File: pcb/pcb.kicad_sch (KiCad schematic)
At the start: 3 parts, among them U2 ESP32-C6-MINI-1

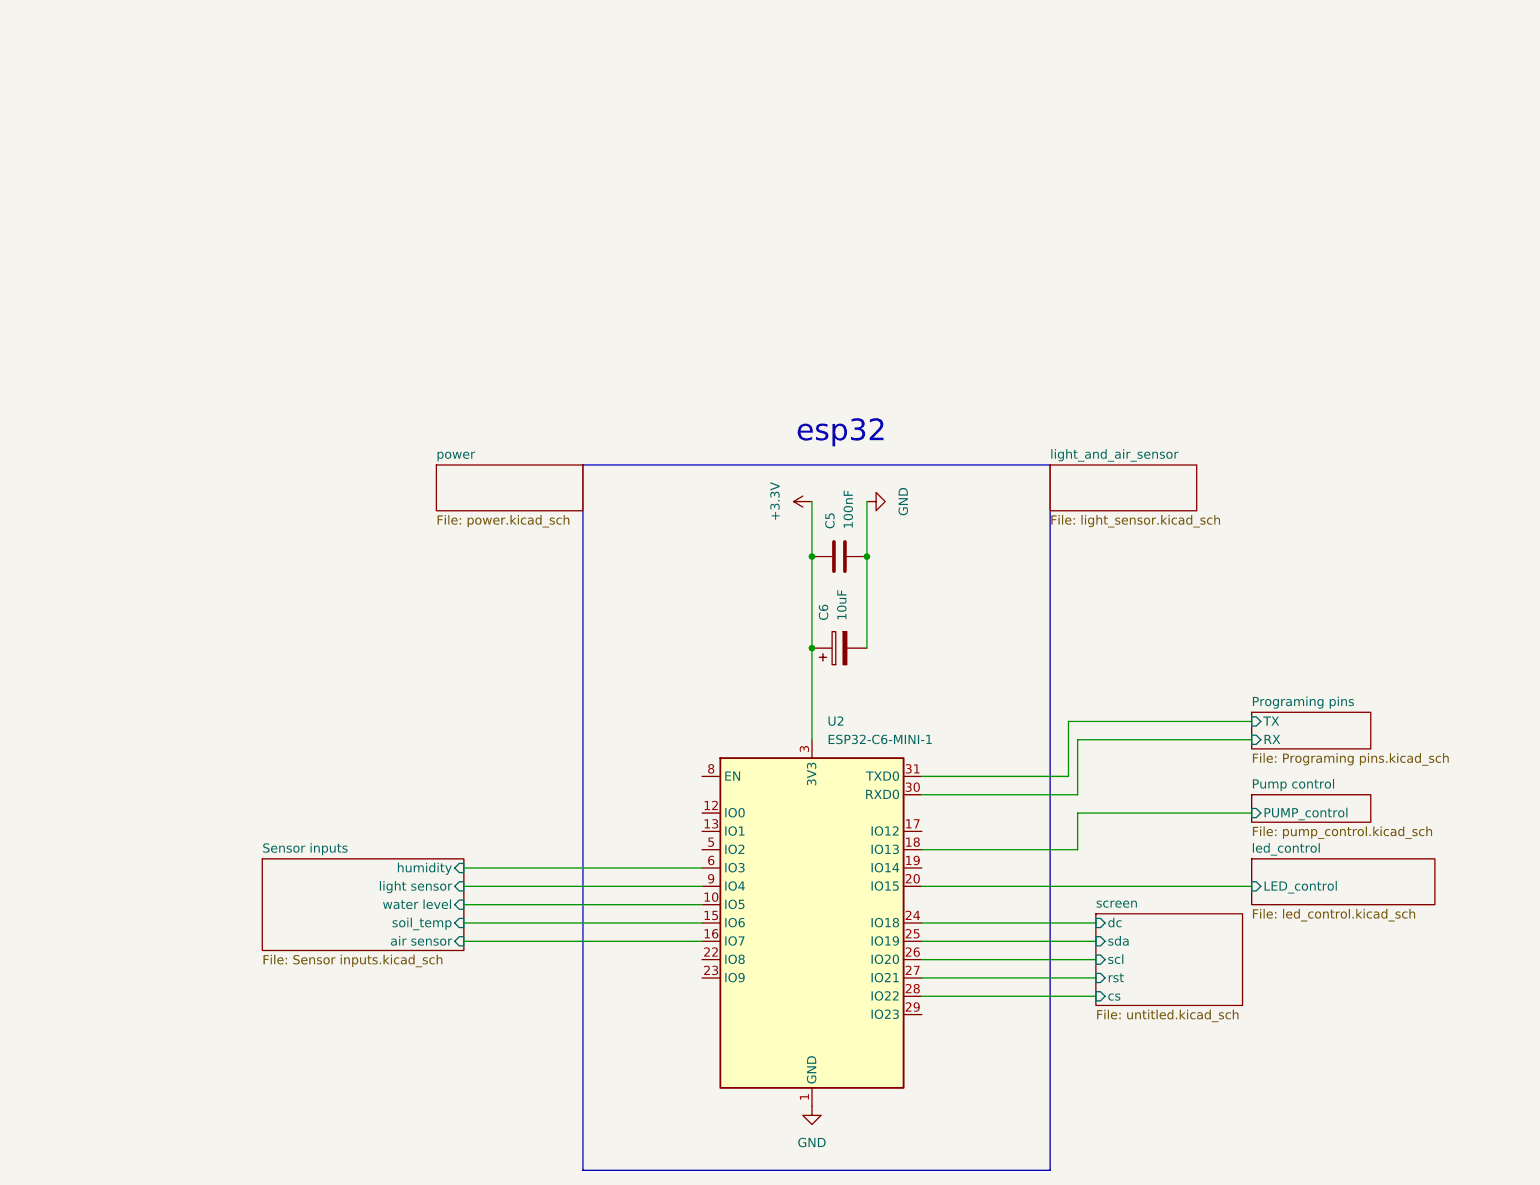
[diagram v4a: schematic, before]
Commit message: trieing to make a 3d model from the shematic and fixing some issues about the esp32 gipos
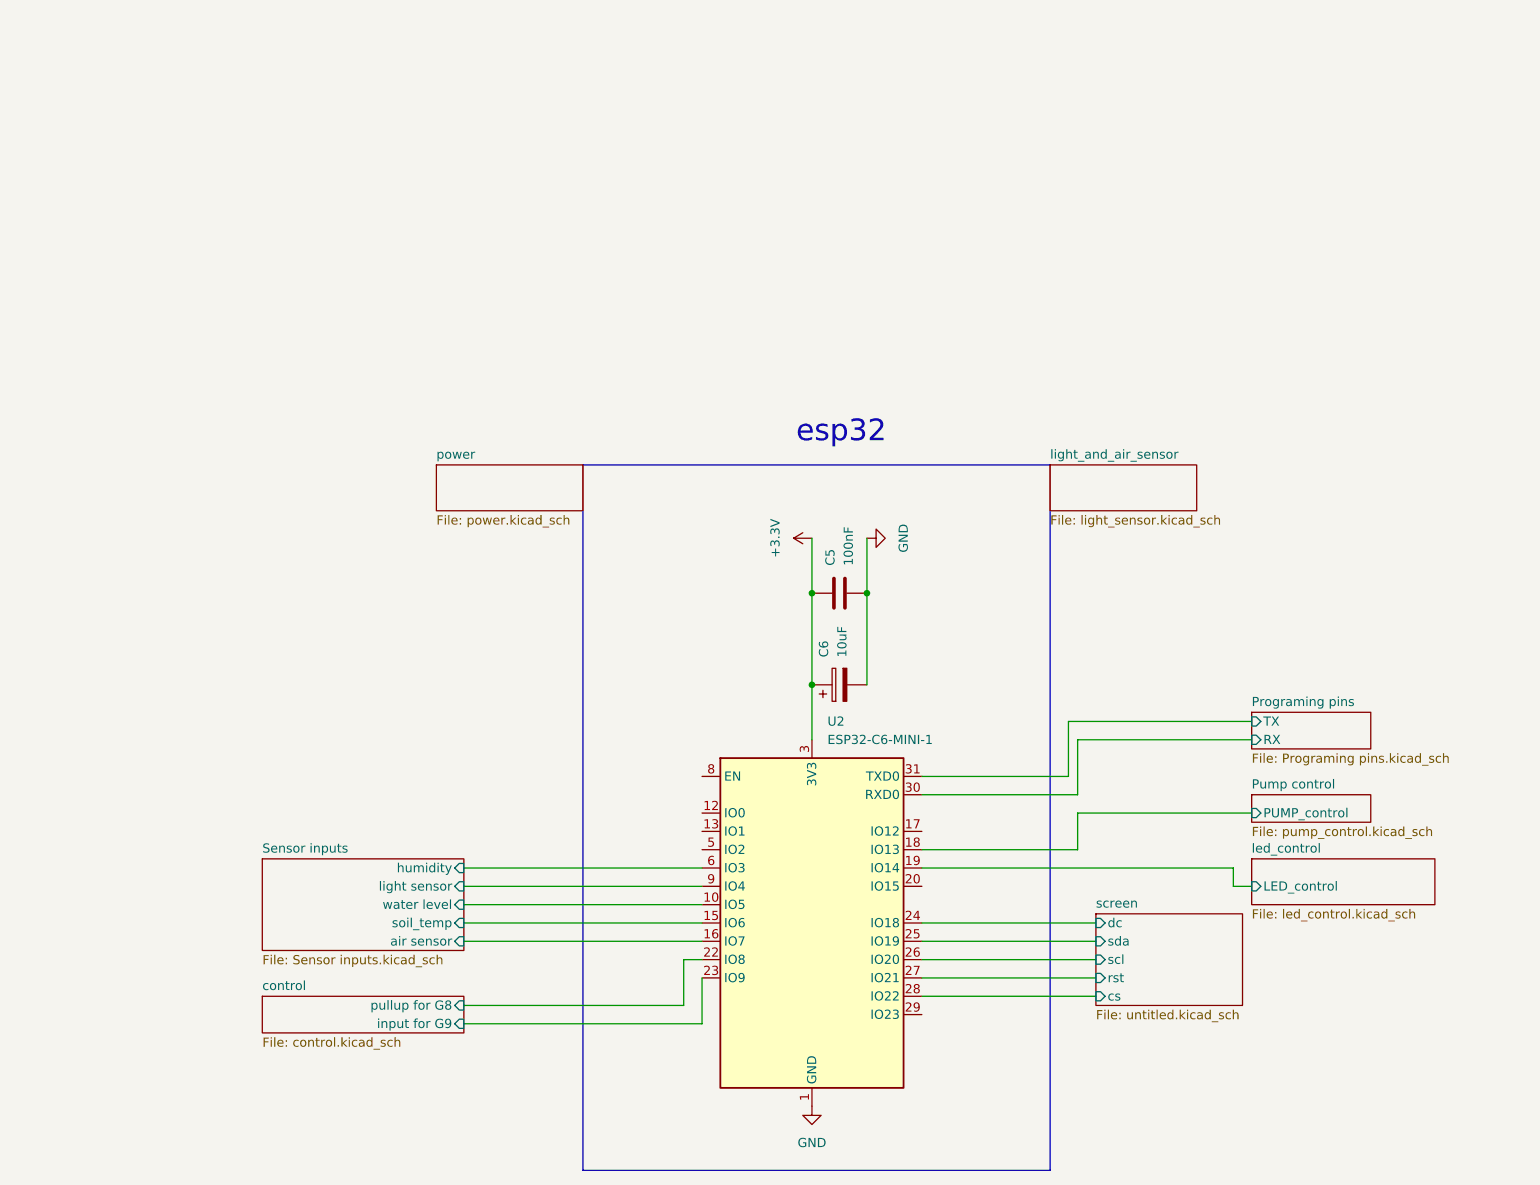
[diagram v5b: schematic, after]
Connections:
- net led_control/LED_control: now also U2.19 (IO14); no longer U2.20 (IO15)
- net control/pullup for G8: now reaches U2.22 (IO8)
- net control/input for G9: now reaches U2.23 (IO9)
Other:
- added sheet control (control.kicad_sch)
- moved on the sheet: C5, C6
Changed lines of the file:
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@@
 	)
 	(junction
-		(at 137.16 91.44)
+		(at 137.16 96.52)
 		(diameter 0)
 		(color 0 0 0 0)
 	)
 	(junction
-		(at 129.54 91.44)
+		(at 129.54 96.52)
 		(diameter 0)
 		(color 0 0 0 0)
 	)
 	(junction
-		(at 129.54 104.14)
+		(at 129.54 109.22)
 		(diameter 0)
 		(color 0 0 0 0)
@@
 	(wire
 		(pts
-			(xy 129.54 104.14) (xy 129.54 116.84)
+			(xy 129.54 109.22) (xy 129.54 116.84)
+		)
+		(stroke
+			(width 0)
+			(type default)
+		)
+	)
+	(wire
+		(pts
+			(xy 111.76 147.32) (xy 111.76 153.67)
 		)
 		(stroke
@@
 	(wire
 		(pts
+			(xy 187.96 134.62) (xy 187.96 137.16)
+		)
+		(stroke
+			(width 0)
+			(type default)
+		)
+	)
+	(wire
+		(pts
 			(xy 166.37 116.84) (xy 166.37 124.46)
 		)
@@
 	(wire
 		(pts
+			(xy 81.28 156.21) (xy 114.3 156.21)
+		)
+		(stroke
+			(width 0)
+			(type default)
+		)
+	)
+	(wire
+		(pts
+			(xy 114.3 147.32) (xy 111.76 147.32)
+		)
+		(stroke
+			(width 0)
+			(type default)
+		)
+	)
+	(wire
+		(pts
+			(xy 187.96 137.16) (xy 190.5 137.16)
+		)
+		(stroke
+			(width 0)
+			(type default)
+		)
+	)
+	(wire
+		(pts
 			(xy 144.78 152.4) (xy 168.91 152.4)
 		)
@@
 	(wire
 		(pts
-			(xy 129.54 91.44) (xy 129.54 104.14)
+			(xy 129.54 96.52) (xy 129.54 109.22)
 		)
 		(stroke
@@
 	(wire
 		(pts
-			(xy 137.16 91.44) (xy 137.16 104.14)
+			(xy 114.3 156.21) (xy 114.3 149.86)
+		)
+		(stroke
+			(width 0)
+			(type default)
+		)
+	)
+	(wire
+		(pts
+			(xy 137.16 96.52) (xy 137.16 109.22)
 		)
 		(stroke
@@
 	(wire
 		(pts
-			(xy 144.78 137.16) (xy 190.5 137.16)
-		)
-		(stroke
-			(width 0)
-			(type default)
-		)
-	)
-	(wire
-		(pts
 			(xy 165.1 114.3) (xy 165.1 121.92)
 		)
@@
 	(wire
 		(pts
-			(xy 129.54 83.82) (xy 129.54 91.44)
-		)
-		(stroke
-			(width 0)
-			(type default)
-		)
-	)
-	(wire
-		(pts
-			(xy 137.16 83.82) (xy 137.16 91.44)
+			(xy 129.54 88.9) (xy 129.54 96.52)
+		)
+		(stroke
+			(width 0)
+			(type default)
+		)
+	)
+	(wire
+		(pts
+			(xy 81.28 153.67) (xy 111.76 153.67)
+		)
+		(stroke
+			(width 0)
+			(type default)
+		)
+	)
+	(wire
+		(pts
+			(xy 144.78 134.62) (xy 187.96 134.62)
+		)
+		(stroke
+			(width 0)
+			(type default)
+		)
+	)
+	(wire
+		(pts
+			(xy 137.16 88.9) (xy 137.16 96.52)
 		)
 		(stroke
@@
 	(symbol
 		(lib_id "power:GND")
-		(at 137.16 83.82 90)
+		(at 137.16 88.9 90)
 		(unit 1)
 		(exclude_from_sim no)
@@
 		(fields_autoplaced yes)
 		(property "Reference" "#PWR04"
-			(at 143.51 83.82 0)
+			(at 143.51 88.9 0)
 			(effects
 				(font
@@
 		)
 		(property "Value" "GND"
-			(at 142.24 83.82 0)
+			(at 142.24 88.9 0)
 			(effects
 				(font
@@
 		)
 		(property "Footprint" ""
-			(at 137.16 83.82 0)
+			(at 137.16 88.9 0)
 			(effects
 				(font
@@
 		)
 		(property "Datasheet" ""
-			(at 137.16 83.82 0)
+			(at 137.16 88.9 0)
 			(effects
 				(font
@@
 		)
 		(property "Description" "Power symbol creates a global label with name \"GND\" , ground"
-			(at 137.16 83.82 0)
+			(at 137.16 88.9 0)
 			(effects
 				(font
@@
 	(symbol
 		(lib_id "Device:C_Polarized")
-		(at 133.35 104.14 90)
+		(at 133.35 109.22 90)
 		(unit 1)
 		(exclude_from_sim no)
@@
 		(fields_autoplaced yes)
 		(property "Reference" "C6"
-			(at 131.1909 100.33 0)
+			(at 131.1909 105.41 0)
 			(effects
 				(font
@@
 		)
 		(property "Value" "10uF"
-			(at 133.7309 100.33 0)
+			(at 133.7309 105.41 0)
 			(effects
 				(font
@@
 		)
 		(property "Footprint" "Capacitor_THT:CP_Radial_D5.0mm_P2.50mm"
-			(at 137.16 103.1748 0)
+			(at 137.16 108.2548 0)
 			(effects
 				(font
@@
 		)
 		(property "Datasheet" "~"
-			(at 133.35 104.14 0)
+			(at 133.35 109.22 0)
 			(effects
 				(font
@@
 		)
 		(property "Description" "Polarized capacitor"
-			(at 133.35 104.14 0)
+			(at 133.35 109.22 0)
 			(effects
 				(font
@@
 		)
 		(property "amazon link" ""
-			(at 133.35 104.14 0)
+			(at 133.35 109.22 0)
 			(effects
 				(font
@@
 		)
 		(property "jlc part #" "C216288"
-			(at 133.35 104.14 0)
+			(at 133.35 109.22 0)
 			(effects
 				(font
@@
 	(symbol
 		(lib_id "Device:C")
-		(at 133.35 91.44 90)
+		(at 133.35 96.52 90)
 		(unit 1)
 		(exclude_from_sim no)
@@
 		(fields_autoplaced yes)
 		(property "Reference" "C5"
-			(at 132.0799 87.63 0)
+			(at 132.0799 92.71 0)
 			(effects
 				(font
@@
 		)
 		(property "Value" "100nF"
-			(at 134.6199 87.63 0)
+			(at 134.6199 92.71 0)
 			(effects
 				(font
@@
 		)
 		(property "Footprint" "Resistor_SMD:R_0603_1608Metric_Pad0.98x0.95mm_HandSolder"
-			(at 137.16 90.4748 0)
+			(at 137.16 95.5548 0)
 			(effects
 				(font
@@
 		)
 		(property "Datasheet" "~"
-			(at 133.35 91.44 0)
+			(at 133.35 96.52 0)
 			(effects
 				(font
@@
 		)
 		(property "Description" "Unpolarized capacitor"
-			(at 133.35 91.44 0)
+			(at 133.35 96.52 0)
 			(effects
 				(font
@@
 		)
 		(property "amazon link" ""
-			(at 133.35 91.44 0)
+			(at 133.35 96.52 0)
 			(effects
 				(font
@@
 		)
 		(property "jlc part #" "C1591"
-			(at 133.35 91.44 0)
+			(at 133.35 96.52 0)
 			(effects
 				(font
@@
 	(symbol
 		(lib_id "power:+3.3V")
-		(at 129.54 83.82 90)
+		(at 129.54 88.9 90)
 		(unit 1)
 		(exclude_from_sim no)
@@
 		(fields_autoplaced yes)
 		(property "Reference" "#PWR03"
-			(at 133.35 83.82 0)
+			(at 133.35 88.9 0)
 			(effects
 				(font
@@
 		)
 		(property "Value" "+3.3V"
-			(at 124.46 83.82 0)
+			(at 124.46 88.9 0)
 			(effects
 				(font
@@
 		)
 		(property "Footprint" ""
-			(at 129.54 83.82 0)
+			(at 129.54 88.9 0)
 			(effects
 				(font
@@
 		)
 		(property "Datasheet" ""
-			(at 129.54 83.82 0)
+			(at 129.54 88.9 0)
 			(effects
 				(font
@@
 		)
 		(property "Description" "Power symbol creates a global label with name \"+3.3V\""
-			(at 129.54 83.82 0)
+			(at 129.54 88.9 0)
 			(effects
 				(font
@@
 				)
 			)
+		)
+	)
+	(sheet
+		(at 53.34 152.4)
+		(size 27.94 5.08)
+		(exclude_from_sim no)
+		(in_bom yes)
+		(on_board yes)
+		(dnp no)
+		(fields_autoplaced yes)
+		(stroke
+			(width 0.1524)
+			(type solid)
+		)
+		(fill
+			(color 0 0 0 0.0000)
+		)
+		(property "Sheetname" "control"
+			(at 53.34 151.6884 0)
+			(effects
+				(font
+					(size 1.27 1.27)
+				)
+				(justify left bottom)
+			)
+		)
+		(property "Sheetfile" "control.kicad_sch"
+			(at 53.34 158.0646 0)
+			(effects
+				(font
+					(size 1.27 1.27)
+				)
+				(justify left top)
+			)
+		)
+		(pin "pullup for G8" input
+			(at 81.28 153.67 0)
+			(effects
+				(font
+					(size 1.27 1.27)
+				)
+				(justify right)
+			)
+		)
+		(pin "input for G9" input
+			(at 81.28 156.21 0)
+			(effects
+				(font
+					(size 1.27 1.27)
+				)
+				(justify right)
+			)
+		)
+		(instances
+			(project "pcb"
+				(path "/2955ee96-3683-4cf6-bfa3-83b5e4980920"
+					(page "9")
+				)
+			)

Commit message: Finding parts and folishing the pcb
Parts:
- C6: footprint Capacitor_THT:CP_Radial_D5.0mm_P2.50mm -> Capacitor_THT:CP_Radial_D5.0mm_P2.00mm
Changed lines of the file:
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@@
 			)
 		)
-		(property "Footprint" "Capacitor_THT:CP_Radial_D5.0mm_P2.50mm"
+		(property "Footprint" "Capacitor_THT:CP_Radial_D5.0mm_P2.00mm"
 			(at 137.16 108.2548 0)
 			(effects

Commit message: separating the usb-c
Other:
- added sheet usbc modul (usb-c.kicad_sch)

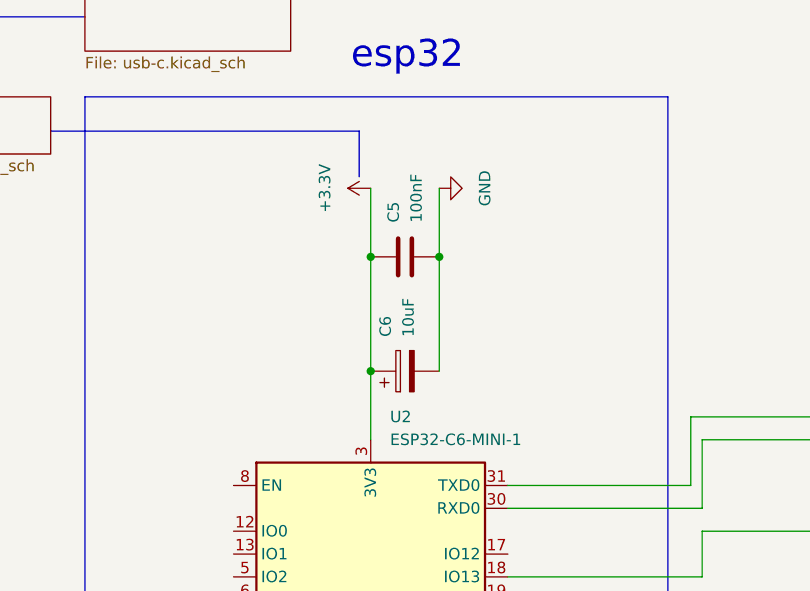
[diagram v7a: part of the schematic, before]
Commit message: Finishing the carrier board with the new usb-c modul
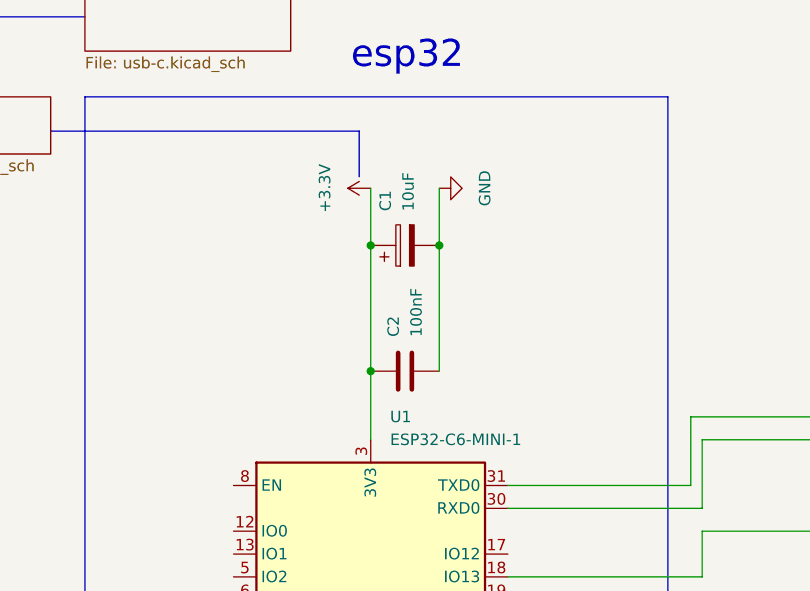
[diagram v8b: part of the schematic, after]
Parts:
- removed C5: 100nF, Resistor_SMD:R_0603_1608Metric_Pad0.98x0.95mm_HandSolder, symbol Device:C
- removed C6: 10uF, Capacitor_THT:CP_Radial_D5.0mm_P2.00mm, symbol Device:C_Polarized
- added C1: 10uF, Capacitor_THT:CP_Radial_D5.0mm_P2.00mm, symbol Device:C_Polarized
- added C2: 100nF, Resistor_SMD:R_0603_1608Metric_Pad0.98x0.95mm_HandSolder, symbol Device:C
- renumbered U2 to U1
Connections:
- net +3.3V: now also C1.1, C2.1
- net GND: now also C1.2, C2.2
